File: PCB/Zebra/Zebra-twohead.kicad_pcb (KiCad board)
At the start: 2 copper layers, 38.1 x 43.2 mm, 9 parts, among them J1 Conn_01x11, J2 MJ-4PP-9, U1 ProMicro, U2 ssd1306

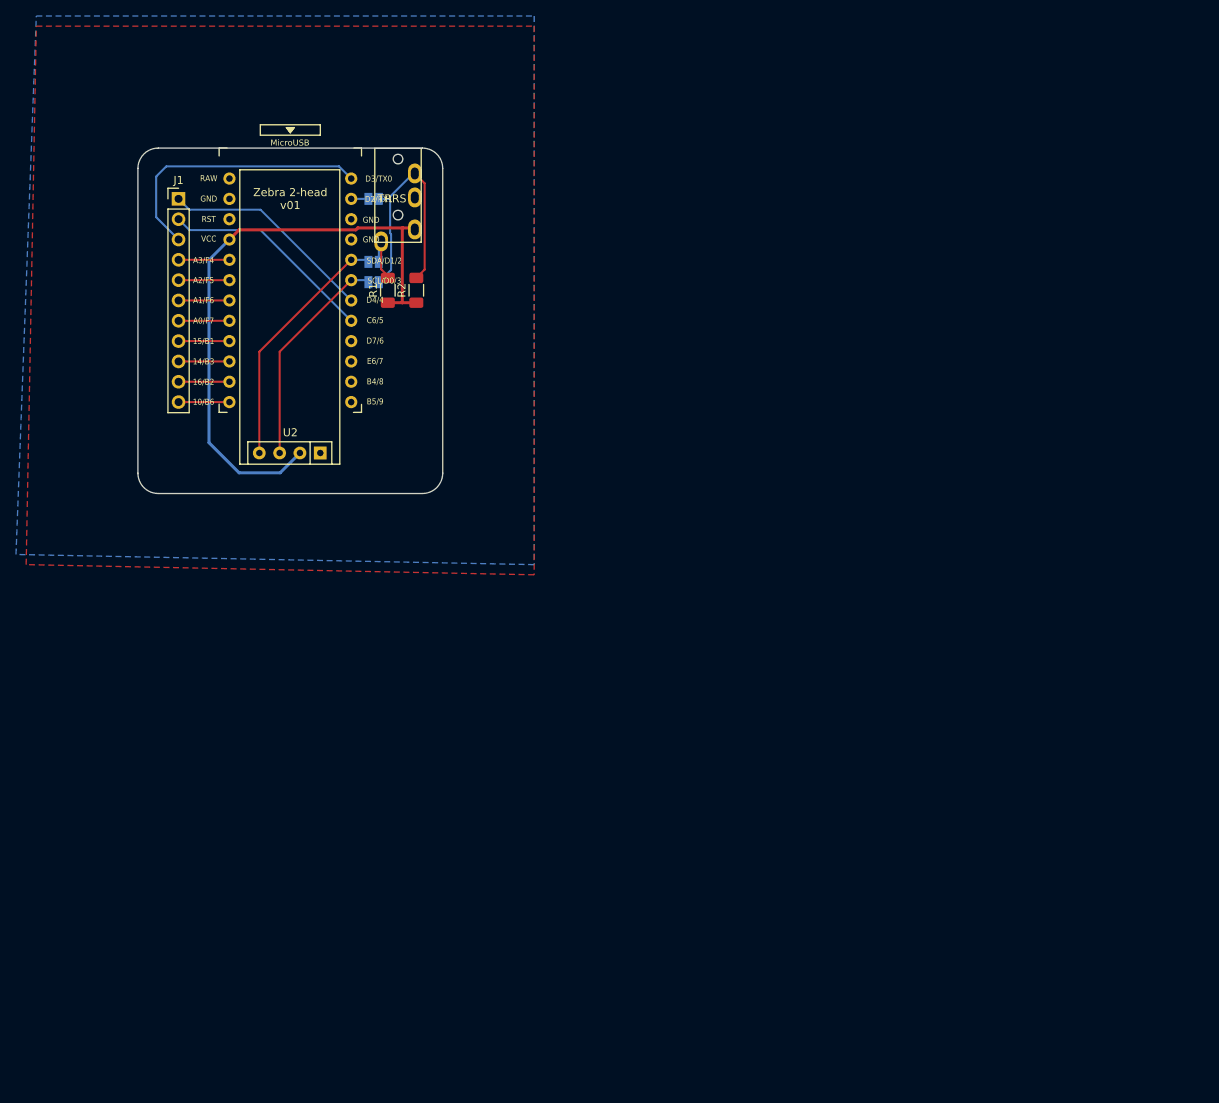
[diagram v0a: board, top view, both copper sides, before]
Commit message: Add extra connector, LED, clean up
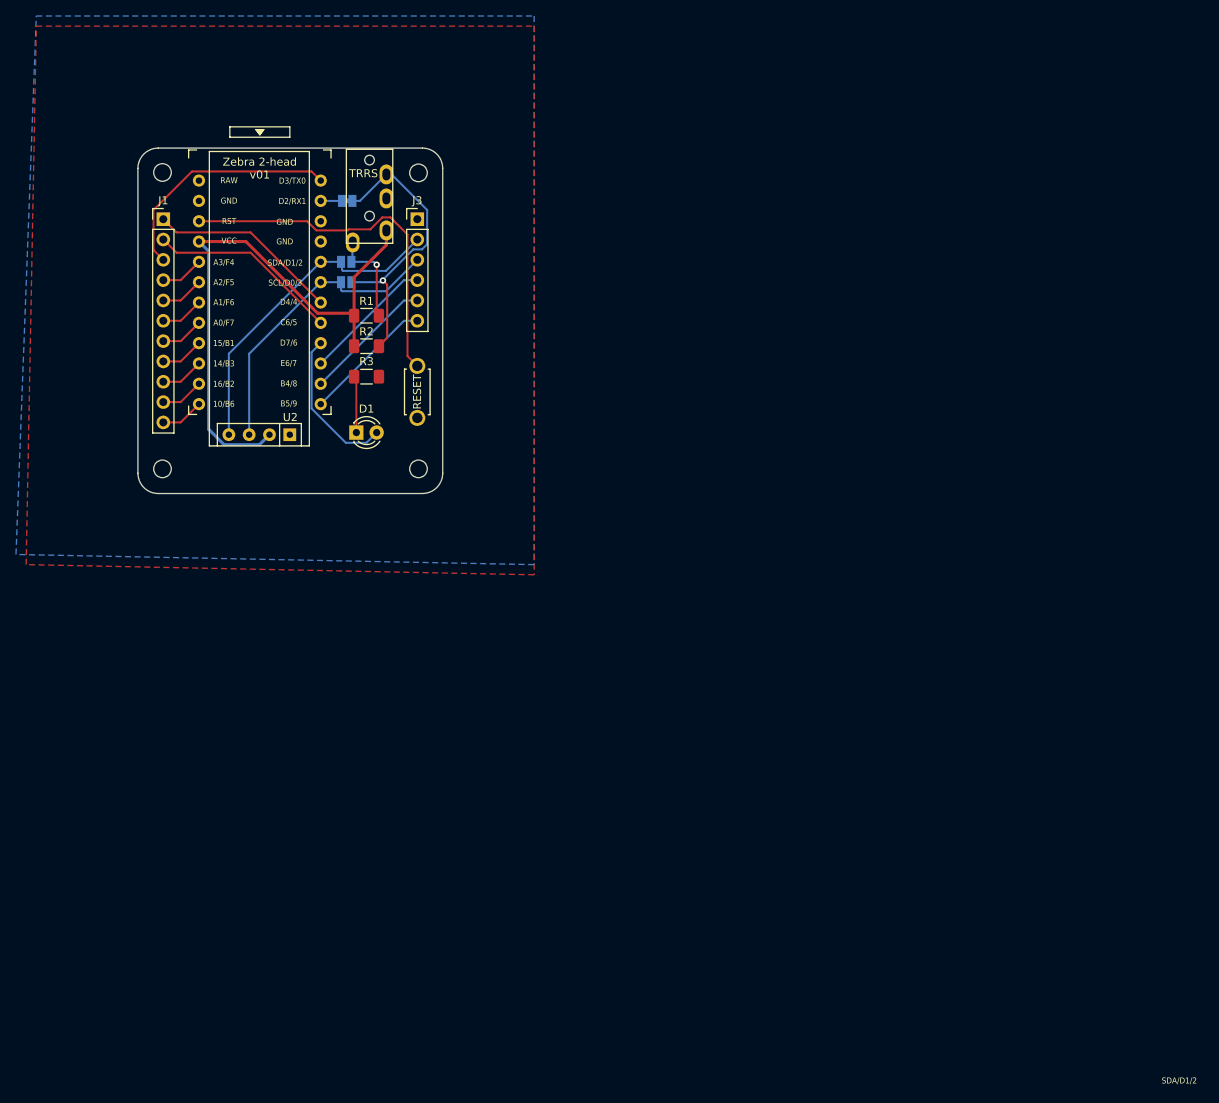
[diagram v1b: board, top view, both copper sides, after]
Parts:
- added ?: , , F.Cu at (95.2, 85.7)
- added D1: LED, LED_THT:LED_D3.0mm, F.Cu at (102.2, 124.5)
- added J3: Conn_01x06, Connector_PinHeader_2.54mm:PinHeader_1x06_P2.54mm_Vertical, F.Cu at (109.9, 97.8)
- added R3: 1k, Resistor_SMD:R_1206_3216Metric_Pad1.30x1.75mm_HandSolder, F.Cu at (103.5, 117.5)
- added REF**: MountingHole_2.2mm_M2, MountingHole:MountingHole_2.2mm_M2, F.Cu at (110.0, 92.0)
- added REF**: MountingHole_2.2mm_M2, MountingHole:MountingHole_2.2mm_M2, F.Cu at (110.0, 129.0)
- added REF**: MountingHole_2.2mm_M2, MountingHole:MountingHole_2.2mm_M2, F.Cu at (78.0, 129.0)
- added REF**: MountingHole_2.2mm_M2, MountingHole:MountingHole_2.2mm_M2, F.Cu at (78.0, 91.9)
- added SW1: SW_Push, kbd:ResetSW_1side, F.Cu at (109.9, 119.4)
- moved R2 9.35 mm to (103.5, 113.7), turned to 0 degrees
- moved U2 4.44 mm to (89.9, 109.7)
- moved R1 4.15 mm to (103.5, 109.9), turned to 0 degrees
- moved U1 3.82 mm to (90.2, 107.4)
- moved J2 3.56 mm to (103.9, 88.9)
- moved JP1 3.43 mm to (101.0, 103.1)
- moved JP2 3.43 mm to (101.0, 105.7)
- moved JP3 3.31 mm to (101.1, 95.5)
- moved J1 3.18 mm to (78.1, 97.8)
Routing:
- net Net-(SW1-Pad1): track 0.00 -> 45.0 mm
- net Net-(D1-Pad2): track 0.00 -> 19.1 mm
- net Net-(J3-Pad6): track 0.00 -> 16.4 mm
- net Net-(J3-Pad5): track 0.00 -> 16.4 mm
- net Net-(J3-Pad4): track 0.00 -> 16.4 mm
- net SCL: track 27.7 -> 37.5 mm
- net SDA: track 31.5 -> 41.1 mm
- net Net-(D1-Pad1): track 0.00 -> 7.10 mm
- net Net-(J2-PadB): track 31.0 -> 37.1 mm, vias 0 -> 1
- net VCC: track 76.9 -> 72.2 mm
- net Net-(J1-Pad3): track 34.6 -> 30.1 mm
- net Net-(J2-PadA): track 7.68 -> 12.1 mm, vias 0 -> 1
- net Net-(J1-Pad1): track 26.9 -> 24.0 mm
- net Net-(J1-Pad2): track 26.9 -> 24.0 mm
- net Net-(J1-Pad8): track 6.35 -> 5.40 mm
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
